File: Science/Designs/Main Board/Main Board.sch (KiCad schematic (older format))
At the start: 102 parts, among them J1 I2C_OUT, J10 AIR_SENS, J11 MOISTURE_SENS, J12 LIMIT3, J13 LIMIT2, J14 LIMIT1, J15 SERVO3, J16 SERVO2, J17 SERVO1, J18 MOTOR1_SIG, J19 MOTOR2_SIG, J2 ANE_SENS, J20 MOTOR3_SIG, J4 ENCODER2, J5 ENCODER1, J7 ATMO_SENS, P1 LS7366R, P2 LS7366R, P3 RPI_HEADER, P4 PWR_IN, P5 UV_SENS, P6 DIST_SENS, P7 I2C_TEST, P8 THERMO_SENS, P9 SPI_TEST, U1 SN74HC14N, U2 TLV2544ID, U3 PCA9685, U4 PCA9685, Y1 20MHz, Y2 20MHz

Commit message: Added 7.2V regulator
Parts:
- added C18: 100nF, symbol C
- added C19: 1µF, symbol C
- added HS1: HEATSINK, symbol HEATSINK
- added R40: 2.2kΩ, symbol R
- added R41: 470Ω, symbol R
- added U7: LM317T, symbol LM317T
- D10, D11, D4, D5, D6, D7, D8, D9: symbol LED_RGB -> LED_RGB-RESCUE-Main_Board
- gave numbers to parts that had none: 9
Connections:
- net labels added: 7.2V
- wire segments 434 -> 446
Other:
- moved on the sheet: C11, P7, P9, U4

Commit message: Schematic cleanup
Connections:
- net LIM1_OUT: now also P3.11 (P11)
- net LIM2_OUT: now also P3.13 (P13)
- net LIM3_OUT: now also P3.15 (P15)
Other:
- moved on the sheet: C1, C18, C19, C2, C3, C4, C5, C6, C7, C8, HS1, J12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

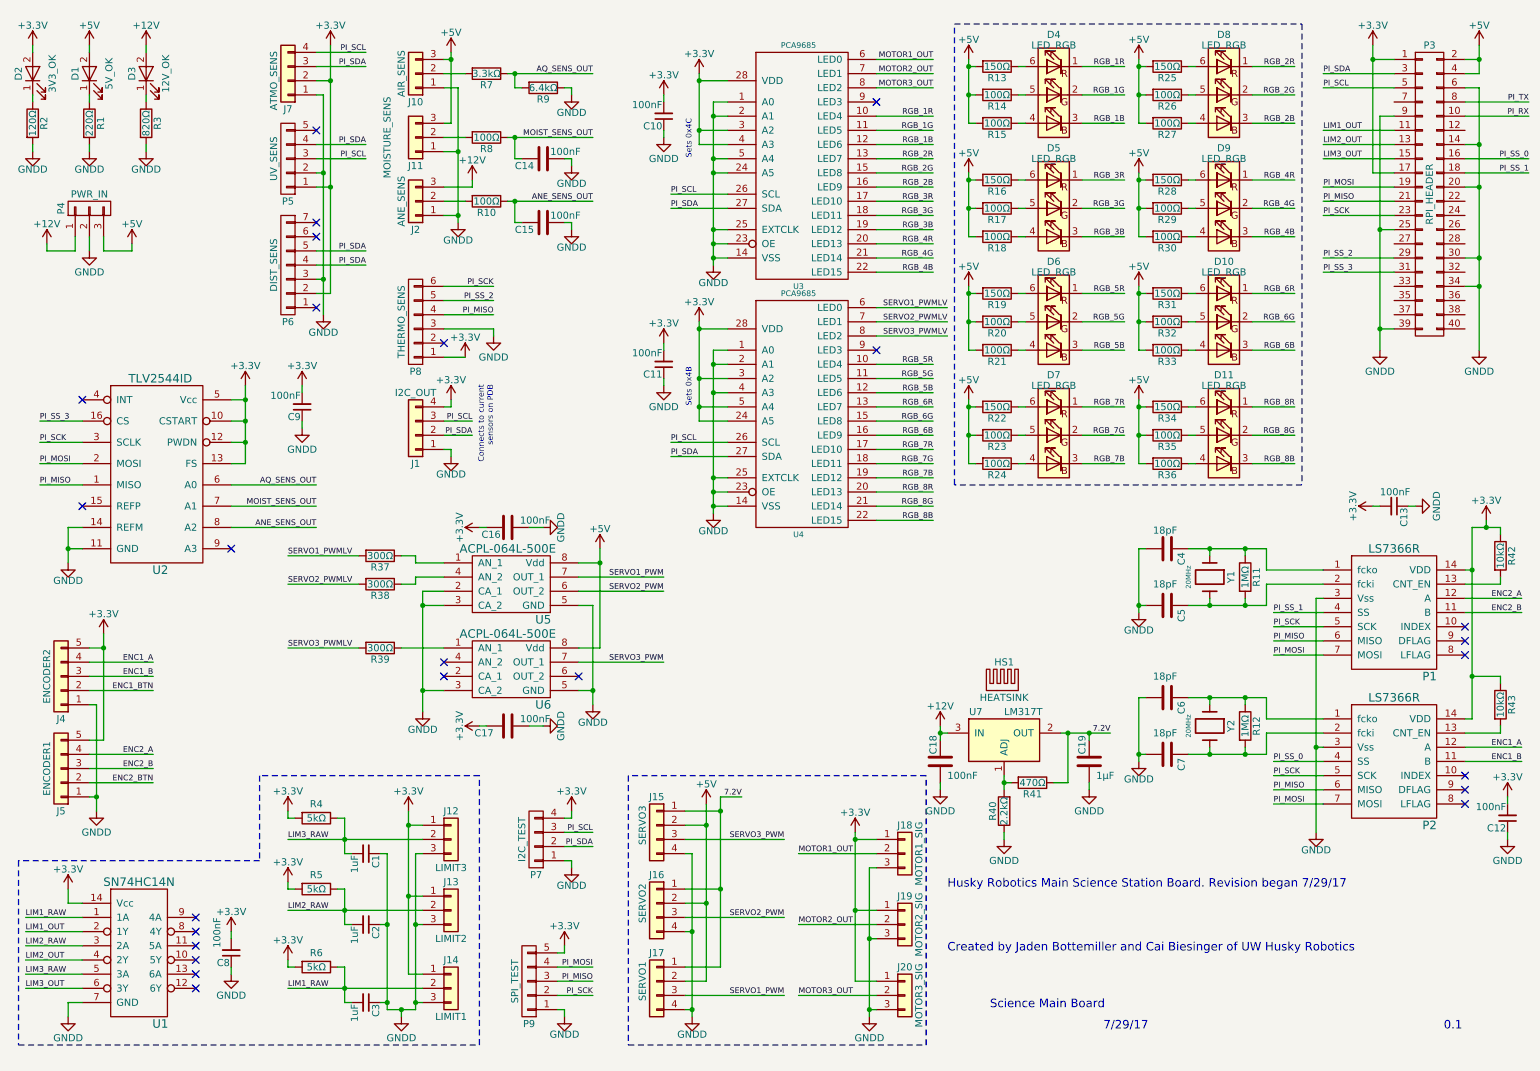
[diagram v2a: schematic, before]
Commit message: Switched to resistor networks for RGB LEDs
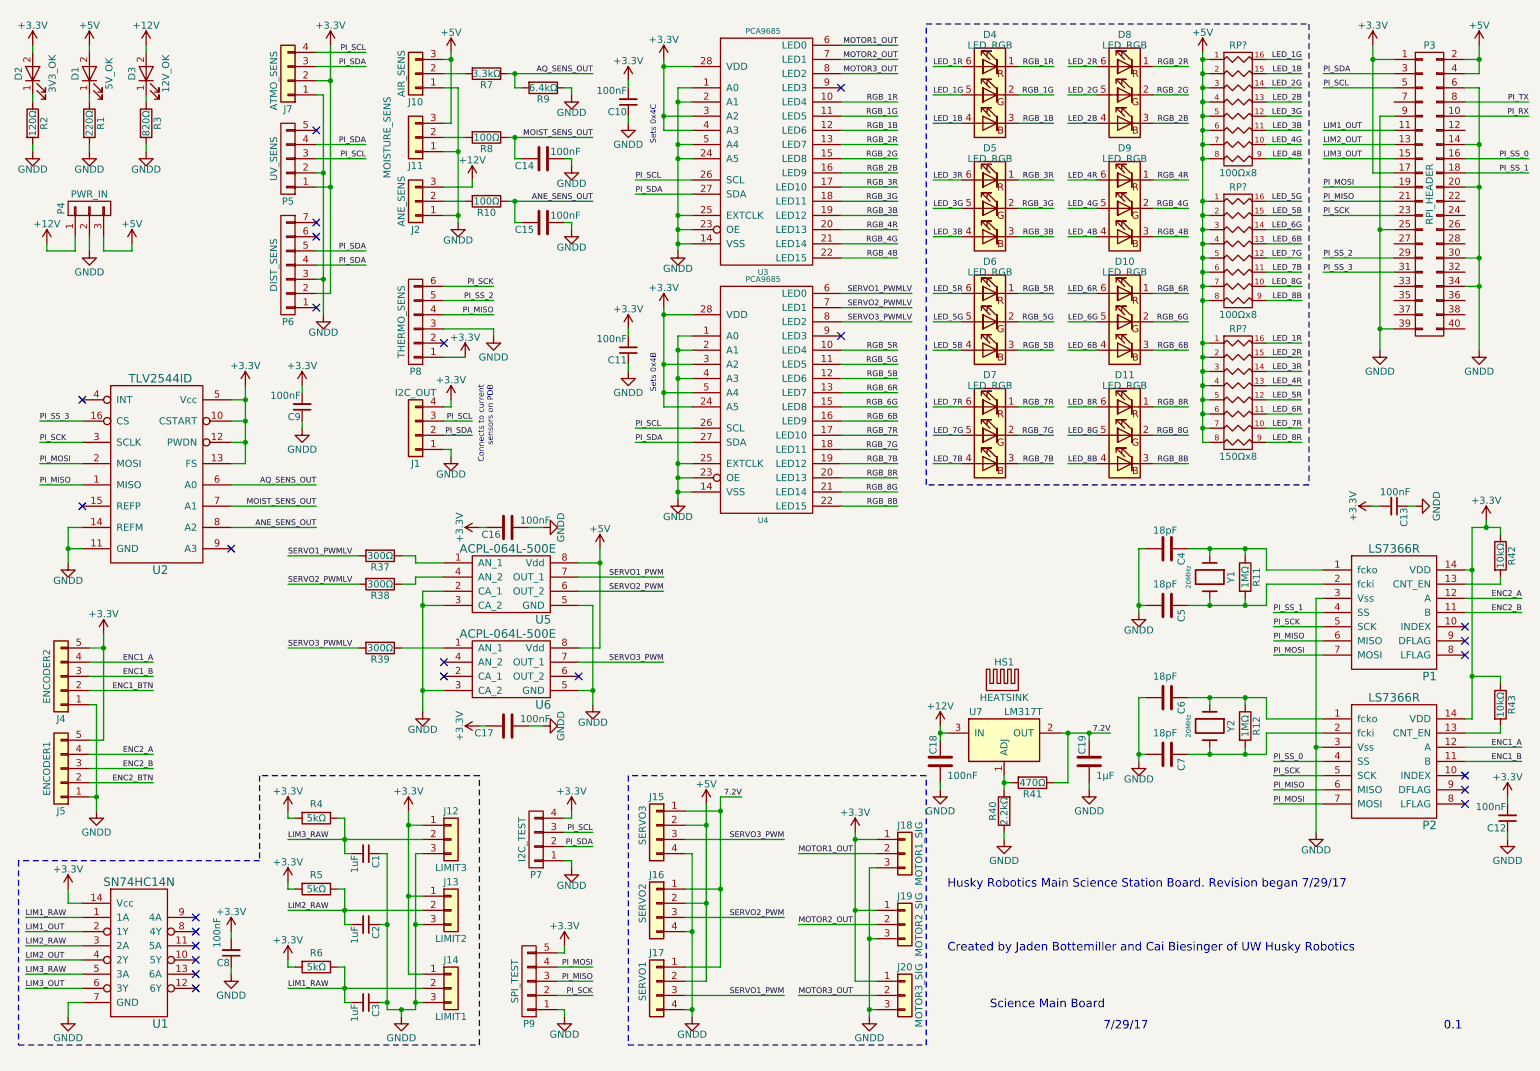
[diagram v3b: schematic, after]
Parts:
- removed R13, R16, R19, R22, R25, R28, R31, R34: 150Ω, Resistors_SMD:R_1206_HandSoldering, symbol R
- removed R14, R15, R17, R18, R20, R21, R23, R24, R26, R27, R29, R30, R32, R33, R35, R36: 100Ω, Resistors_SMD:R_1206_HandSoldering, symbol R
- added RP? (x2): 100Ωx8, symbol R_PACK8
- added RP?: 150Ωx8, symbol R_PACK8
- C14, C15, C16, C17, C18, C19: footprint (none) -> Capacitors_SMD:C_1206_HandSoldering
- D1, D2, D3: footprint (none) -> LEDs:LED_D5.0mm
- J1, J15, J16, J17, J7: footprint (none) -> ScienceFootprints:MOLEX_22-23-2041
- J10, J11, J12, J13, J14, J18, J19, J2, J20: footprint (none) -> ScienceFootprints:MOLEX_22-23-2031
- J4, J5, P5: footprint (none) -> ScienceFootprints:MOLEX_22-23-2051
- P6: footprint (none) -> ScienceFootprints:MOLEX_22-23-2071
- P7: footprint (none) -> Pin_Headers:Pin_Header_Straight_1x04_Pitch2.54mm
- P8: footprint (none) -> ScienceFootprints:MOLEX_22-23-2061
- P9: footprint (none) -> Pin_Headers:Pin_Header_Straight_1x05_Pitch2.54mm
- R37, R38, R39, R40, R41, R42, R43: footprint (none) -> Resistors_SMD:R_1206_HandSoldering
- U7: footprint (none) -> TO_SOT_Packages_THT:TO-220-3_Vertical
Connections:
- net +5V: now also RP?.1 (P1), RP?.1 (P1), RP?.1 (P1), RP?.2 (P2), RP?.2 (P2), RP?.2 (P2), RP?.3 (P3), RP?.3 (P3), RP?.3 (P3), RP?.4 (P4), RP?.4 (P4), RP?.4 (P4), RP?.5 (P5), RP?.5 (P5), RP?.5 (P5), RP?.6 (P6), RP?.6 (P6), RP?.6 (P6), RP?.7 (P7), RP?.7 (P7), RP?.7 (P7), RP?.8 (P8), RP?.8 (P8), RP?.8 (P8)
- net LED_1B: now reaches D4.4 (BA)
- net LED_1B: now also RP?.15 (R2)
- net LED_1G: now reaches D4.5 (GA)
- net LED_1G: now also RP?.16 (R1)
- net LED_1R: now reaches D4.6 (RA)
- net LED_1R: now also RP?.16 (R1)
- net LED_3B: now reaches D5.4 (BA)
- net LED_3B: now also RP?.11 (R6)
- net LED_3G: now reaches D5.5 (GA)
- net LED_3G: now also RP?.12 (R5)
- net LED_3R: now reaches D5.6 (RA)
- net LED_3R: now also RP?.14 (R3)
- net LED_5B: now reaches D6.4 (BA)
- net LED_5B: now also RP?.15 (R2)
- net LED_5G: now reaches D6.5 (GA)
- net LED_5G: now also RP?.16 (R1)
- net LED_5R: now reaches D6.6 (RA)
- net LED_5R: now also RP?.12 (R5)
- net LED_7B: now reaches D7.4 (BA)
- net LED_7B: now also RP?.11 (R6)
- net LED_7G: now reaches D7.5 (GA)
- net LED_7G: now also RP?.12 (R5)
- net LED_7R: now reaches D7.6 (RA)
- net LED_7R: now also RP?.10 (R7)
- net LED_2B: now reaches D8.4 (BA)
- net LED_2B: now also RP?.13 (R4)
- net LED_2G: now reaches D8.5 (GA)
- net LED_2G: now also RP?.14 (R3)
- net LED_2R: now reaches D8.6 (RA)
- net LED_2R: now also RP?.15 (R2)
- net LED_4B: now reaches D9.4 (BA)
- net LED_4B: now also RP?.9 (R8)
- net LED_4G: now reaches D9.5 (GA)
- net LED_4G: now also RP?.10 (R7)
- net LED_4R: now reaches D9.6 (RA)
- net LED_4R: now also RP?.13 (R4)
- net LED_6B: now reaches D10.4 (BA)
- net LED_6B: now also RP?.13 (R4)
- net LED_6G: now reaches D10.5 (GA)
- net LED_6G: now also RP?.14 (R3)
- net LED_6R: now reaches D10.6 (RA)
- net LED_6R: now also RP?.11 (R6)
- net LED_8B: now reaches D11.4 (BA)
- net LED_8B: now also RP?.9 (R8)
- net LED_8G: now reaches D11.5 (GA)
- net LED_8G: now also RP?.10 (R7)
- net LED_8R: now reaches D11.6 (RA)
- net LED_8R: now also RP?.9 (R8)
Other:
- moved on the sheet: C10, C11, D10, D11, D4, D5, D6, D7, D8, D9, U3, U4

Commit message: Continued working on main PCB
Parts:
- added D12: 7V2_OK, LEDs:LED_D5.0mm, symbol LED-RESCUE-Main_Board
- added R13: 270Ω, Resistors_SMD:R_1206_HandSoldering, symbol R
- P1, P2, U1: footprint (none) -> Housings_SOIC:SOIC-14_3.9x8.7mm_Pitch1.27mm
- RP1, RP2, RP3: renamed from RP?; footprint (none) -> Housings_SOIC:SOIC-16_3.9x9.9mm_Pitch1.27mm
- U2: footprint (none) -> Housings_SOIC:SOIC-16_3.9x9.9mm_Pitch1.27mm
- U3, U4: footprint (none) -> Housings_SSOP:TSSOP-28_4.4x9.7mm_Pitch0.65mm
- U5, U6: footprint (none) -> Housings_SOIC:SOIC-8_3.9x4.9mm_Pitch1.27mm
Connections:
- net 7.2V: now also D12.2 (A)
- net GNDD: now also R13.2
- new net: D12.1 (K), R13.1
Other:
- moved on the sheet: D3, R3

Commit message: Working on PCB
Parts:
- D10, D11, D4, D5, D6, D7, D8, D9: footprint (none) -> ScienceFootprints:SLV6A-FKB
- P3: footprint (none) -> ScienceFootprints:RPi-3B
- P4: footprint (none) -> ScienceFootprints:PHOENIX_1792232
- Y1, Y2: footprint (none) -> ScienceFootprints:HC-49USX
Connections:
- net +3V3: no longer C16.1, C17.1
- net +5V: now also C16.1, C17.1
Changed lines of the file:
@@
 F 0 "P3" H 10450 2800 50  0000 C CNN
 F 1 "RPI_HEADER" V 10450 1750 50  0000 C CNN
-F 2 "" H 10450 800 50  0001 C CNN
+F 2 "ScienceFootprints:RPi-3B" H 10450 800 50  0001 C CNN
 F 3 "" H 10450 800 50  0000 C CNN
 	1    10450 1750
@@
 F 0 "Y1" H 8900 4600 50  0000 C CNN
 F 1 "20MHz" H 8900 4300 35  0000 C CNN
-F 2 "" H 8900 4450 50  0001 C CNN
+F 2 "ScienceFootprints:HC-49USX" H 8900 4450 50  0001 C CNN
 F 3 "" H 8900 4450 50  0001 C CNN
 	1    8900 4450
@@
 F 0 "Y2" H 8900 5650 50  0000 C CNN
 F 1 "20MHz" H 8900 5350 35  0000 C CNN
-F 2 "" H 8900 5500 50  0001 C CNN
+F 2 "ScienceFootprints:HC-49USX" H 8900 5500 50  0001 C CNN
 F 3 "" H 8900 5500 50  0001 C CNN
 	1    8900 5500
@@
 F 0 "D4" H 7350 1475 50  0000 C CNN
 F 1 "LED_RGB" H 7350 1400 50  0000 C CNN
-F 2 "" H 7350 1000 50  0001 C CNN
+F 2 "ScienceFootprints:SLV6A-FKB" H 7350 1000 50  0001 C CNN
 F 3 "" H 7350 1000 50  0000 C CNN
 	1    7350 1050
@@
 F 0 "D5" H 7350 2275 50  0000 C CNN
 F 1 "LED_RGB" H 7350 2200 50  0000 C CNN
-F 2 "" H 7350 1800 50  0001 C CNN
+F 2 "ScienceFootprints:SLV6A-FKB" H 7350 1800 50  0001 C CNN
 F 3 "" H 7350 1800 50  0000 C CNN
 	1    7350 1850
@@
 F 0 "D6" H 7350 3075 50  0000 C CNN
 F 1 "LED_RGB" H 7350 3000 50  0000 C CNN
-F 2 "" H 7350 2600 50  0001 C CNN
+F 2 "ScienceFootprints:SLV6A-FKB" H 7350 2600 50  0001 C CNN
 F 3 "" H 7350 2600 50  0000 C CNN
 	1    7350 2650
@@
 F 0 "D7" H 7350 3875 50  0000 C CNN
 F 1 "LED_RGB" H 7350 3800 50  0000 C CNN
-F 2 "" H 7350 3400 50  0001 C CNN
+F 2 "ScienceFootprints:SLV6A-FKB" H 7350 3400 50  0001 C CNN
 F 3 "" H 7350 3400 50  0000 C CNN
 	1    7350 3450
@@
 F 0 "D8" H 8300 1475 50  0000 C CNN
 F 1 "LED_RGB" H 8300 1400 50  0000 C CNN
-F 2 "" H 8300 1000 50  0001 C CNN
+F 2 "ScienceFootprints:SLV6A-FKB" H 8300 1000 50  0001 C CNN
 F 3 "" H 8300 1000 50  0000 C CNN
 	1    8300 1050
@@
 F 0 "D9" H 8300 2275 50  0000 C CNN
 F 1 "LED_RGB" H 8300 2200 50  0000 C CNN
-F 2 "" H 8300 1800 50  0001 C CNN
+F 2 "ScienceFootprints:SLV6A-FKB" H 8300 1800 50  0001 C CNN
 F 3 "" H 8300 1800 50  0000 C CNN
 	1    8300 1850
@@
 F 0 "D10" H 8300 3075 50  0000 C CNN
 F 1 "LED_RGB" H 8300 3000 50  0000 C CNN
-F 2 "" H 8300 2600 50  0001 C CNN
+F 2 "ScienceFootprints:SLV6A-FKB" H 8300 2600 50  0001 C CNN
 F 3 "" H 8300 2600 50  0000 C CNN
 	1    8300 2650
@@
 F 0 "D11" H 8300 3875 50  0000 C CNN
 F 1 "LED_RGB" H 8300 3800 50  0000 C CNN
-F 2 "" H 8300 3400 50  0001 C CNN
+F 2 "ScienceFootprints:SLV6A-FKB" H 8300 3400 50  0001 C CNN
 F 3 "" H 8300 3400 50  0000 C CNN
 	1    8300 3450
@@
 F 0 "P4" H 1000 2050 50  0000 C CNN
 F 1 "PWR_IN" V 1100 1850 50  0000 C CNN
-F 2 "" H 1000 1850 50  0001 C CNN
+F 2 "ScienceFootprints:PHOENIX_1792232" H 1000 1850 50  0001 C CNN
 F 3 "" H 1000 1850 50  0000 C CNN
 	1    1000 1850
@@
 	1    0    0    -1
 $EndComp
-$Comp
-L +3.3V #PWR066
-U 1 1 5A5A9802
-P 3750 4100
-F 0 "#PWR066" H 3750 3950 50  0001 C CNN
-F 1 "+3.3V" H 3750 4240 50  0000 C CNN
-F 2 "" H 3750 4100 50  0001 C CNN
-F 3 "" H 3750 4100 50  0001 C CNN
-	1    3750 4100
-	0    -1   -1   0
-$EndComp
 Wire Wire Line
 	3750 4100 3800 4100
@@
 NoConn ~ 2000 4250
 $Comp
-L +3.3V #PWR068
-U 1 1 5A5AC227
-P 3750 5500
-F 0 "#PWR068" H 3750 5350 50  0001 C CNN
-F 1 "+3.3V" H 3750 5640 50  0000 C CNN
-F 2 "" H 3750 5500 50  0001 C CNN
-F 3 "" H 3750 5500 50  0001 C CNN
-	1    3750 5500
-	0    -1   -1   0
-$EndComp
-$Comp
 L C C17
 U 1 1 5A5AC22E
@@
 Wire Wire Line
 	1400 1400 1400 1450
+$Comp
+L +5V #PWR?
+U 1 1 5A5B2E2D
+P 3750 4100
+F 0 "#PWR?" H 3750 3950 50  0001 C CNN
+F 1 "+5V" H 3750 4240 50  0000 C CNN
+F 2 "" H 3750 4100 50  0001 C CNN
+F 3 "" H 3750 4100 50  0001 C CNN
+	1    3750 4100
+	0    -1   -1   0
+$EndComp
+$Comp
+L +5V #PWR?
+U 1 1 5A5B2F43
+P 3750 5500
+F 0 "#PWR?" H 3750 5350 50  0001 C CNN
+F 1 "+5V" H 3750 5640 50  0000 C CNN
+F 2 "" H 3750 5500 50  0001 C CNN
+F 3 "" H 3750 5500 50  0001 C CNN
+	1    3750 5500
+	0    -1   -1   0
+$EndComp
 $EndSCHEMATC

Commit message: Finishing up for tonight.
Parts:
- HS1: footprint (none) -> ScienceFootprints:AAVID_531202B02500G
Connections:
- net PI_SCL: now also P6.5 (P5)
- net PI_SDA: no longer P6.5 (P5)
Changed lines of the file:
@@
 PI_SDA
 Text Label 2950 2150 2    40   ~ 0
-PI_SDA
+PI_SCL
 NoConn ~ 2600 2050
 NoConn ~ 2600 1950
@@
 	4100 4100 4200 4100
 $Comp
-L GNDD #PWR067
+L GNDD #PWR066
 U 1 1 5A5AA55C
 P 4200 4100
-F 0 "#PWR067" H 4200 3850 50  0001 C CNN
+F 0 "#PWR066" H 4200 3850 50  0001 C CNN
 F 1 "GNDD" H 4200 3975 50  0000 C CNN
 F 2 "" H 4200 4100 50  0001 C CNN
@@
 $EndComp
 $Comp
-L GNDD #PWR069
+L GNDD #PWR067
 U 1 1 5A5AC235
 P 4200 5500
-F 0 "#PWR069" H 4200 5250 50  0001 C CNN
+F 0 "#PWR067" H 4200 5250 50  0001 C CNN
 F 1 "GNDD" H 4200 5375 50  0000 C CNN
 F 2 "" H 4200 5500 50  0001 C CNN
@@
 SERVO1_PWMLV
 $Comp
-L GNDD #PWR070
+L GNDD #PWR068
 U 1 1 5A5B2B6F
 P 3350 5400
-F 0 "#PWR070" H 3350 5150 50  0001 C CNN
+F 0 "#PWR068" H 3350 5150 50  0001 C CNN
 F 1 "GNDD" H 3350 5275 50  0000 C CNN
 F 2 "" H 3350 5400 50  0001 C CNN
@@
 NoConn ~ 10700 6050
 $Comp
-L +5V #PWR071
+L +5V #PWR069
 U 1 1 5A5B9C1F
 P 4600 4250
-F 0 "#PWR071" H 4600 4100 50  0001 C CNN
+F 0 "#PWR069" H 4600 4100 50  0001 C CNN
 F 1 "+5V" H 4600 4390 50  0000 C CNN
 F 2 "" H 4600 4250 50  0001 C CNN
@@
 $EndComp
 $Comp
-L +12V #PWR072
+L +12V #PWR070
 U 1 1 5A5FE053
 P 7000 5500
-F 0 "#PWR072" H 7000 5350 50  0001 C CNN
+F 0 "#PWR070" H 7000 5350 50  0001 C CNN
 F 1 "+12V" H 7000 5640 50  0000 C CNN
 F 2 "" H 7000 5500 50  0000 C CNN
@@
 $EndComp
 $Comp
-L GNDD #PWR073
+L GNDD #PWR071
 U 1 1 5A5FE733
 P 7000 5950
-F 0 "#PWR073" H 7000 5700 50  0001 C CNN
+F 0 "#PWR071" H 7000 5700 50  0001 C CNN
 F 1 "GNDD" H 7000 5800 50  0000 C CNN
 F 2 "" H 7000 5950 50  0000 C CNN
@@
 $EndComp
 $Comp
-L GNDD #PWR074
+L GNDD #PWR072
 U 1 1 5A602FE8
 P 7450 6300
-F 0 "#PWR074" H 7450 6050 50  0001 C CNN
+F 0 "#PWR072" H 7450 6050 50  0001 C CNN
 F 1 "GNDD" H 7450 6150 50  0000 C CNN
 F 2 "" H 7450 6300 50  0000 C CNN
@@
 Connection ~ 8050 5550
 $Comp
-L GNDD #PWR075
+L GNDD #PWR073
 U 1 1 5A604B59
 P 8050 5950
-F 0 "#PWR075" H 8050 5700 50  0001 C CNN
+F 0 "#PWR073" H 8050 5700 50  0001 C CNN
 F 1 "GNDD" H 8050 5800 50  0000 C CNN
 F 2 "" H 8050 5950 50  0000 C CNN
@@
 F 0 "HS1" H 7450 5450 50  0000 C CNN
 F 1 "HEATSINK" H 7450 5200 50  0000 C CNN
-F 2 "" H 7450 5250 50  0001 C CNN
+F 2 "ScienceFootprints:AAVID_531202B02500G" H 7450 5250 50  0001 C CNN
 F 3 "" H 7450 5250 50  0000 C CNN
 	1    7450 5250
@@
 $EndComp
 $Comp
-L +5V #PWR076
+L +5V #PWR074
 U 1 1 5A652FA4
 P 8850 750
-F 0 "#PWR076" H 8850 600 50  0001 C CNN
+F 0 "#PWR074" H 8850 600 50  0001 C CNN
 F 1 "+5V" H 8850 890 50  0000 C CNN
 F 2 "" H 8850 750 50  0000 C CNN
@@
 $EndComp
 $Comp
-L GNDD #PWR077
+L GNDD #PWR075
 U 1 1 5A673D25
 P 1400 1450
-F 0 "#PWR077" H 1400 1200 50  0001 C CNN
+F 0 "#PWR075" H 1400 1200 50  0001 C CNN
 F 1 "GNDD" H 1400 1325 50  0000 C CNN
 F 2 "" H 1400 1450 50  0001 C CNN
@@
 	1400 1400 1400 1450
 $Comp
-L +5V #PWR?
+L +5V #PWR076
 U 1 1 5A5B2E2D
 P 3750 4100
-F 0 "#PWR?" H 3750 3950 50  0001 C CNN
+F 0 "#PWR076" H 3750 3950 50  0001 C CNN
 F 1 "+5V" H 3750 4240 50  0000 C CNN
 F 2 "" H 3750 4100 50  0001 C CNN
@@
 $EndComp
 $Comp
-L +5V #PWR?
+L +5V #PWR077
 U 1 1 5A5B2F43
 P 3750 5500
-F 0 "#PWR?" H 3750 5350 50  0001 C CNN
+F 0 "#PWR077" H 3750 5350 50  0001 C CNN
 F 1 "+5V" H 3750 5640 50  0000 C CNN
 F 2 "" H 3750 5500 50  0001 C CNN

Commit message: Layout nearing completion.
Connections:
- net PI_SS_0: now also P3.31 (P31); no longer P3.16 (P16)
- net PI_SS_1: now also P3.29 (P29); no longer P3.18 (P18)
- net PI_SS_2: now also P3.18 (P18); no longer P3.29 (P29)
- net PI_SS_3: now also P3.16 (P16); no longer P3.31 (P31)
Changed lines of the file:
@@
 PI_SCK
 Text Label 11150 1500 2    40   ~ 0
-PI_SS_0
+PI_SS_3
 Text Label 11150 1600 2    40   ~ 0
-PI_SS_1
+PI_SS_2
 Text Label 9350 4700 0    40   ~ 0
 PI_SS_1
@@
 	10200 2300 9700 2300
 Text Label 9700 2200 0    40   ~ 0
-PI_SS_2
+PI_SS_1
 Text Label 9700 2300 0    40   ~ 0
-PI_SS_3
+PI_SS_0
 Text Label 650  3350 0    40   ~ 0
 PI_SS_3
